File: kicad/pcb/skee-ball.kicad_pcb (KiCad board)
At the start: 2 copper layers, 87 parts, among them J1 SPEAKER_P, J10 NHD_RW, J11 NHD_DB1, J12 NHD_DB0, J13 US_TRIG0, J14 US_TRIG1, J15 US_TRIG2, J16 US_TRIG3, J17 US_TRIG4, J18 US_ECHO0_5, J19 US_ECHO1_5, J2 SPEAKER_N, J20 US_ECH02_5, J21 US_ECHO3_5, J22 US_ECHO4_5, J23 NHD_E1, J24 NHD_E2, J25 NHD_VDD, J26 PWM_SERVO_6, J27 PWM_DC (TIM17_CH1), J28 +24V, J29 NHD_V0, J3 NHD_DB7, J30 BUTTON_P, J31 BUTTON_N, J32 GND, J33 HEADER_GND, J34 HEADER_SWDIO, J35 HEADER_SWCLK, J36 ADC_IN1, J37 3.3, J38 GND, J39 6, J4 NHD_DB6, J40 GND, J41 NHD_VSS, J42 NHD_LED-, J43 NHD_LED+, J5 NHD_DB5, J6 NHD_DB4, J7 NHD_DB3, J8 NHD_DB2, J9 NHD_RS, U1 D24V22F6, U10 LD1117S33TR_SOT223, U11 LD1117S33TR_SOT223, U12 LD1117S33TR_SOT223, U13 LD1117S33TR_SOT223, U14 LD1117S33TR_SOT223, U2 MAX98357A, U3 D24V22F5, U4 STM32F091RCTx, U5 74HC595, U6 74HC595, U7 74LS08, U8 LD1117S33TR_SOT223, U9 LD1117S33TR_SOT223

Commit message: begin routing on pcb
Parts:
- C1, C2, C3, C4, C5, C6, C8: footprint Capacitor_SMD:CP_Elec_3x5.3 -> Capacitor_SMD:C_0805_2012Metric_Pad1.18x1.45mm_HandSolder
- C7, C9: footprint Capacitor_SMD:CP_Elec_3x5.4 -> Capacitor_SMD:C_0805_2012Metric_Pad1.18x1.45mm_HandSolder
- J1, J10, J11, J12, J13, J14, J15, J16, J17, J18, J19, J2, J20, J21, J22, J23, J24, J25, J26, J27, J29, J3, J30, J33, J34, J35, J36, J37, J38, J39, J4, J40, J41, J42, J43, J5, J6, J7, J8, J9: footprint Connector_PinHeader_1.00mm:PinHeader_1x01_P1.00mm_Vertical -> Connector_PinHeader_2.54mm:PinHeader_1x01_P2.54mm_Vertical
- R1, R10, R11, R2, R3, R4, R5, R6, R7, R8, R9, RV1: footprint Resistor_SMD:R_0201_0603Metric -> Resistor_SMD:R_0805_2012Metric_Pad1.20x1.40mm_HandSolder
- moved J22 199.1 mm to (209.5, 55.5)
- moved J21 196.5 mm to (209.5, 51.9)
- moved J20 194.1 mm to (209.5, 48.3)
- moved J19 192.5 mm to (209.5, 44.7)
- moved J18 191.6 mm to (209.5, 41.1)
- moved J33 183.9 mm to (80.2, 86.0)
- moved J34 183.9 mm to (80.2, 79.4)
- moved J35 183.9 mm to (80.2, 82.5)
- moved U12 153.6 mm to (186.9, 76.9), turned to 180 degrees
- moved U11 153.2 mm to (187.0, 65.6), turned to 180 degrees
- moved U10 153.0 mm to (186.9, 54.9), turned to 180 degrees
- moved U9 152.8 mm to (186.8, 43.9), turned to 180 degrees
- moved U8 152.6 mm to (186.7, 33.3), turned to 180 degrees
- moved J13 119.9 mm to (80.2, 61.4)
- moved D5 113.2 mm to (144.8, 65.5)
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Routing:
- net Net-(J22-Pin_1): track 0.00 -> 29.5 mm
- net Net-(J21-Pin_1): track 0.00 -> 24.2 mm
- net Net-(J18-Pin_1): track 0.00 -> 23.8 mm
- net Net-(J20-Pin_1): track 0.00 -> 21.3 mm
- net Net-(J19-Pin_1): track 0.00 -> 20.8 mm

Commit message: added ground plane and some via connections
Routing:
- net GND: track 0.00 -> 129.5 mm, vias 0 -> 13
- added copper zone on B.Cu, net GND

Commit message: update pcb
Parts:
- removed J27: PWM_DC (TIM17_CH1), Connector_PinHeader_2.54mm:PinHeader_1x01_P2.54mm_Vertical
- added C10: 100nF, Capacitor_SMD:C_0805_2012Metric_Pad1.18x1.45mm_HandSolder, B.Cu at (138.4, 64.8)
- added C11: 4.7uF, Capacitor_SMD:C_0805_2012Metric_Pad1.18x1.45mm_HandSolder, B.Cu at (131.7, 61.1)
- added C12: 100nF, Capacitor_SMD:C_0805_2012Metric_Pad1.18x1.45mm_HandSolder, B.Cu at (131.7, 64.4)
- added C14: 100nF, Capacitor_SMD:C_0805_2012Metric_Pad1.18x1.45mm_HandSolder, B.Cu at (138.5, 80.6)
- added C16: 100nF, Capacitor_SMD:C_0805_2012Metric_Pad1.18x1.45mm_HandSolder, B.Cu at (127.3, 75.9)
- added C17: 4.7uF, Capacitor_SMD:C_0805_2012Metric_Pad1.18x1.45mm_HandSolder, B.Cu at (124.6, 76.0)
- added C18: 10nF, Capacitor_SMD:C_0805_2012Metric_Pad1.18x1.45mm_HandSolder, B.Cu at (143.4, 70.4)
- added C19: 1uF, Capacitor_SMD:C_0805_2012Metric_Pad1.18x1.45mm_HandSolder, B.Cu at (145.5, 70.4)
- added J44: HEADER_RST, Connector_PinHeader_2.54mm:PinHeader_1x01_P2.54mm_Vertical, F.Cu at (189.2, 76.2)
- added J45: ULTRASONIC_POWER, Connector_PinHeader_2.54mm:PinHeader_2x05_P2.54mm_Vertical, F.Cu at (124.4, 53.1)
- added J47: DC_GND, Connector_PinHeader_2.54mm:PinHeader_1x01_P2.54mm_Vertical, F.Cu at (55.2, 87.6)
- added J48: PWM_DC, Connector_PinHeader_2.54mm:PinHeader_1x01_P2.54mm_Vertical, F.Cu at (59.9, 87.6)
- added R12: 0, Resistor_SMD:R_0805_2012Metric_Pad1.20x1.40mm_HandSolder, B.Cu at (147.3, 81.3)
- J31: footprint Connector_PinHeader_1.00mm:PinHeader_1x01_P1.00mm_Vertical -> Connector_PinHeader_2.54mm:PinHeader_1x01_P2.54mm_Vertical
- R1: moved to B.Cu
- RV1: footprint Resistor_SMD:R_0805_2012Metric_Pad1.20x1.40mm_HandSolder -> Potentiometer_THT:Potentiometer_Bourns_3339P_Vertical
- U5, U6: footprint Package_SO:SSOP-16_5.3x6.2mm_P0.65mm -> 74HC595N:SOT38-4_NXP
- U7: footprint Package_SO:SSOP-16_5.3x6.2mm_P0.65mm -> SN74LS08N:N14
- moved J26 233.9 mm to (44.3, 87.6), turned to -90 degrees
- moved J39 231.4 mm to (48.0, 87.6), turned to -90 degrees
- moved J40 229.3 mm to (51.6, 87.6), turned to -90 degrees
- moved U7 193.1 mm to (61.6, 73.6), turned to 90 degrees
- moved D8 153.6 mm to (71.5, 76.8)
- moved D6 153.5 mm to (71.5, 73.8)
- moved R10 151.7 mm to (67.6, 77.2)
- moved R8 147.7 mm to (67.6, 73.3)
- moved D7 122.1 mm to (113.8, 53.1), turned to 90 degrees
- moved R11 114.2 mm to (112.4, 81.8)
- moved D9 110.2 mm to (115.6, 82.3)
- moved R9 107.2 mm to (113.9, 56.5), turned to 90 degrees
- moved D4 86.6 mm to (131.7, 86.1), turned to 90 degrees
- moved R6 82.4 mm to (131.7, 82.9), turned to -90 degrees
- moved D1 81.5 mm to (135.5, 86.1), turned to 90 degrees
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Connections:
- net /nRST renamed NRST
- R3 pad 1: PB0 -> PB5
- R4 pad 1: PB1 -> PB6
- R5 pad 1: PB2 -> PB7
- U4 pad 12: GND -> Net-(U4-VSSA)
- U4 pad 13: VDA -> VDD
- U4 pad 25: US_ECHO4_1.1 -> US_ECHO4_3.3
- U4 pad 26: PB0 -> unconnected-(U4-PB0-Pad26)
- U4 pad 27: PB1 -> unconnected-(U4-PB1-Pad27)
- U4 pad 28: PB2 -> unconnected-(U4-PB2-Pad28)
- U4 pad 58: unconnected-(U4-PB6-Pad58) -> PB6
- U4 pad 59: unconnected-(U4-PB7-Pad59) -> PB7
- U4 pad 62: Net-(J27-Pin_1) -> PWM_DC
- U7 pad 1: +6V -> GND
- U7 pad 11: unconnected-(U7-Pad11) -> Net-(J26-Pin_1)
- U7 pad 12: GND -> PWM_SERVO_3.3
- U7 pad 13: GND -> +6V
- U7 pad 2: PWM_SERVO_3.3 -> GND
- U7 pad 3: Net-(J26-Pin_1) -> unconnected-(U7-Pad3)
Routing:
- net GND: track 129.5 -> 20.9 mm, vias 13 -> 2
- net Net-(J11-Pin_1): track 0.00 -> 41.3 mm
- net Net-(J22-Pin_1): track 29.5 -> 0.00 mm
- net Net-(J21-Pin_1): track 24.2 -> 0.00 mm
- net Net-(J18-Pin_1): track 23.8 -> 0.02 mm
- net Net-(J12-Pin_1): track 0.00 -> 22.6 mm
- net Net-(J9-Pin_1): track 0.00 -> 21.5 mm
- net Net-(J20-Pin_1): track 21.3 -> 0.01 mm
- net Net-(J19-Pin_1): track 20.8 -> 0.00 mm
- net Net-(J10-Pin_1): track 0.00 -> 6.09 mm
- net PB3: track 0.00 -> 5.86 mm
- net PB7: track 0.00 -> 5.85 mm
- net Net-(J3-Pin_1): track 0.00 -> 5.65 mm
- net Net-(J8-Pin_1): track 0.00 -> 5.24 mm
- net Net-(J4-Pin_1): track 0.00 -> 5.19 mm
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- added copper zone on F.Cu, net +5V

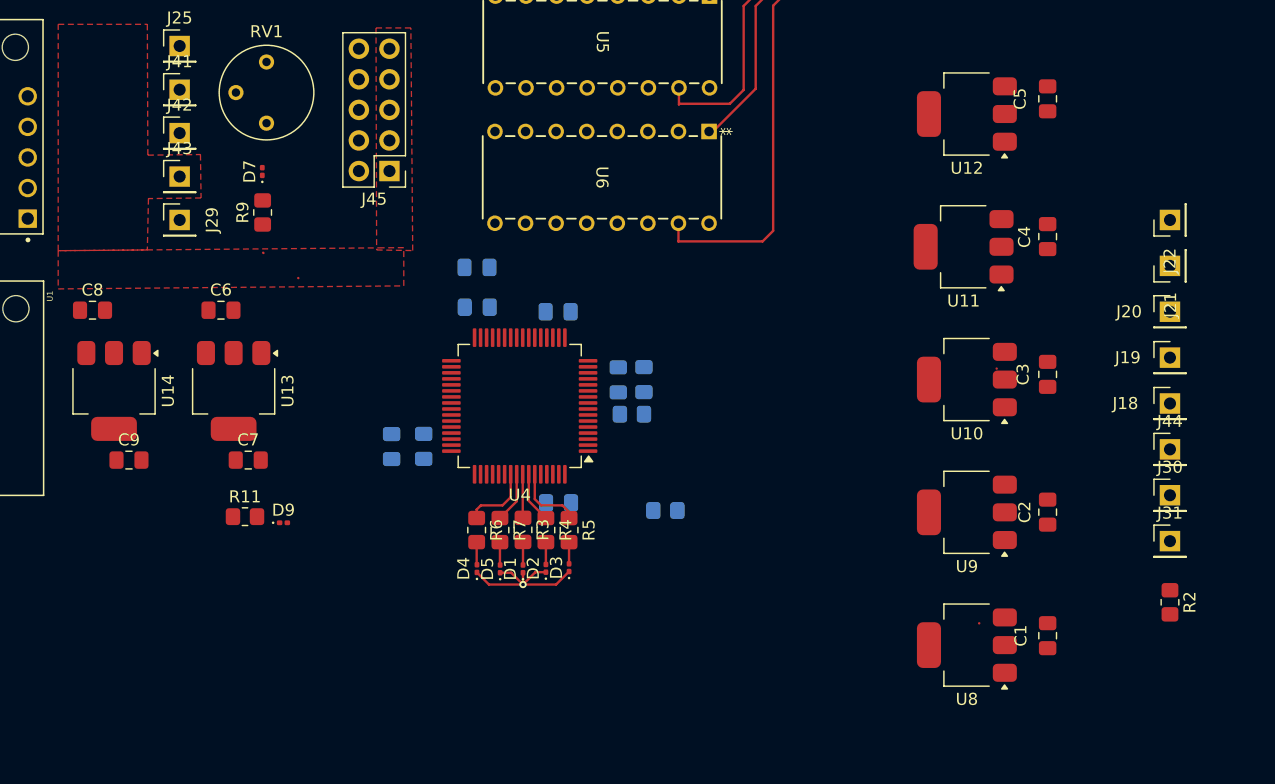
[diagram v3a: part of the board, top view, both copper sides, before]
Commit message: transition to level shifters
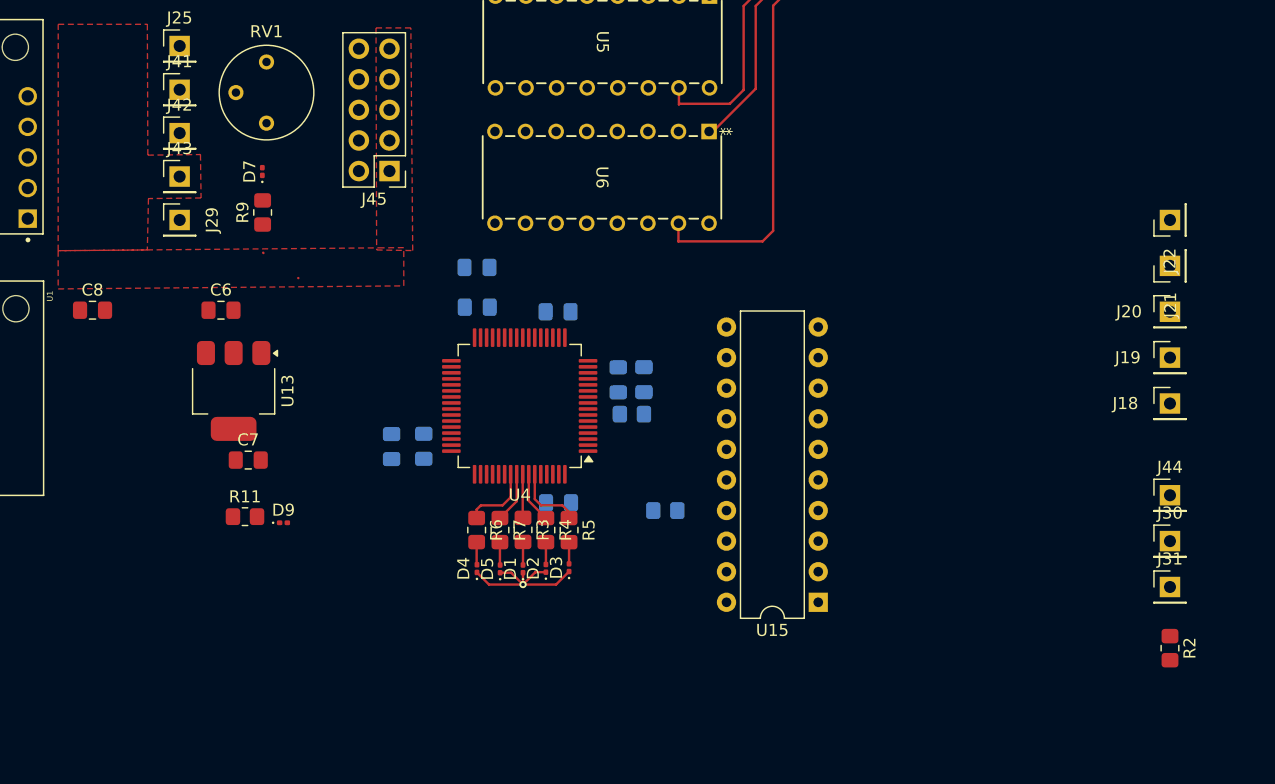
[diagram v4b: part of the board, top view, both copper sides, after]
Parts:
- removed C1, C2, C3, C4, C5: 100nF, Capacitor_SMD:C_0805_2012Metric_Pad1.18x1.45mm_HandSolder
- removed C9: 10uF, Capacitor_SMD:C_0805_2012Metric_Pad1.18x1.45mm_HandSolder
- removed U10, U11, U12, U14, U8, U9: LD1117S33TR_SOT223, Package_TO_SOT_SMD:SOT-223-3_TabPin2
- added U15: 74AHCT541, Package_DIP:DIP-20_W7.62mm, F.Cu at (160.0, 88.9)
- moved J31 3.81 mm to (189.2, 87.6)
- moved J44 3.81 mm to (189.2, 80.0)
- moved J30 3.81 mm to (189.2, 83.8)
- moved R2 3.81 mm to (189.2, 92.7)
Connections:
- U4 pad 10: US_ECHO1_3.3 -> US_ECHO2_3.3
- U4 pad 11: US_ECHO2_3.3 -> US_ECHO1_3.3
- U4 pad 13: VDD -> VDDA
- U4 pad 14: unconnected-(U4-PA0-Pad14) -> US_ECHO0_3.3
- U4 pad 24: US_ECHO3_3.3 -> unconnected-(U4-PC4-Pad24)
- U4 pad 25: US_ECHO4_3.3 -> unconnected-(U4-PC5-Pad25)
- U4 pad 8: unconnected-(U4-PC0-Pad8) -> US_ECHO4_3.3
- U4 pad 9: US_ECHO0_3.3 -> US_ECHO3_3.3

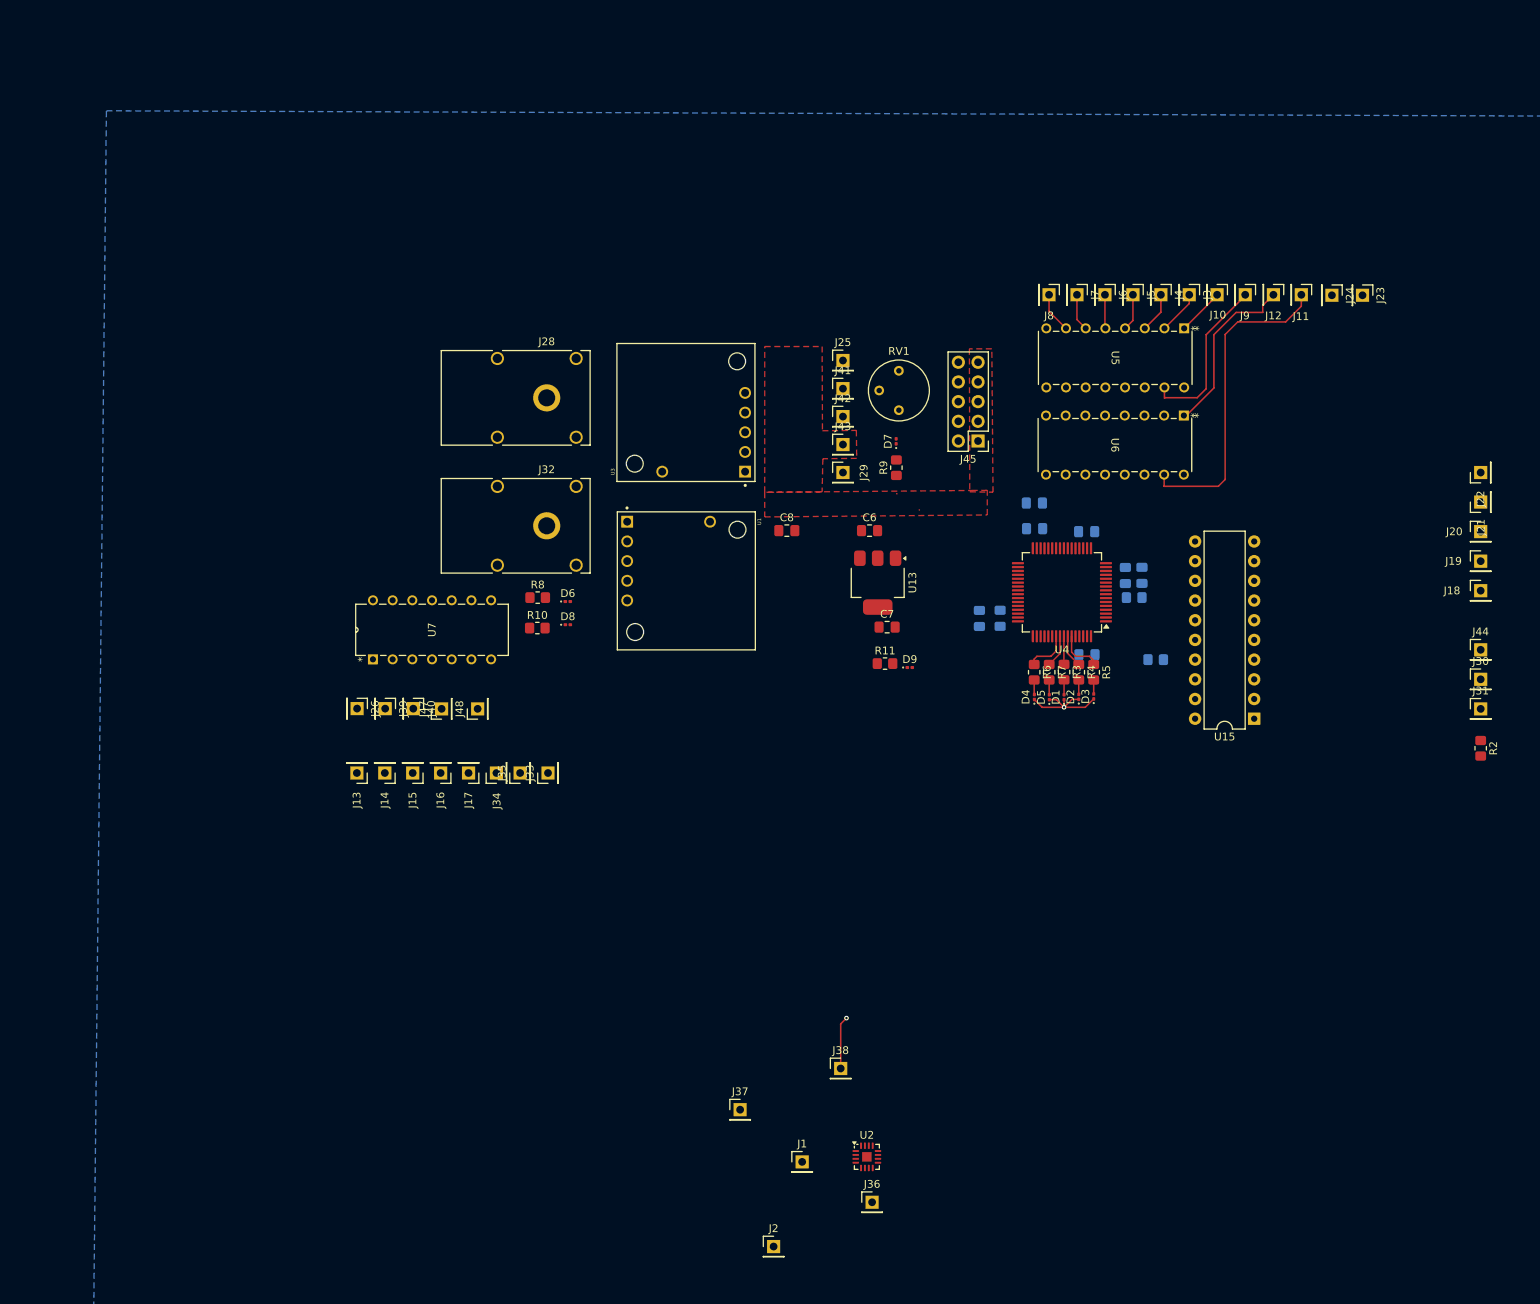
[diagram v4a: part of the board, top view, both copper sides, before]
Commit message: add new connector footprints
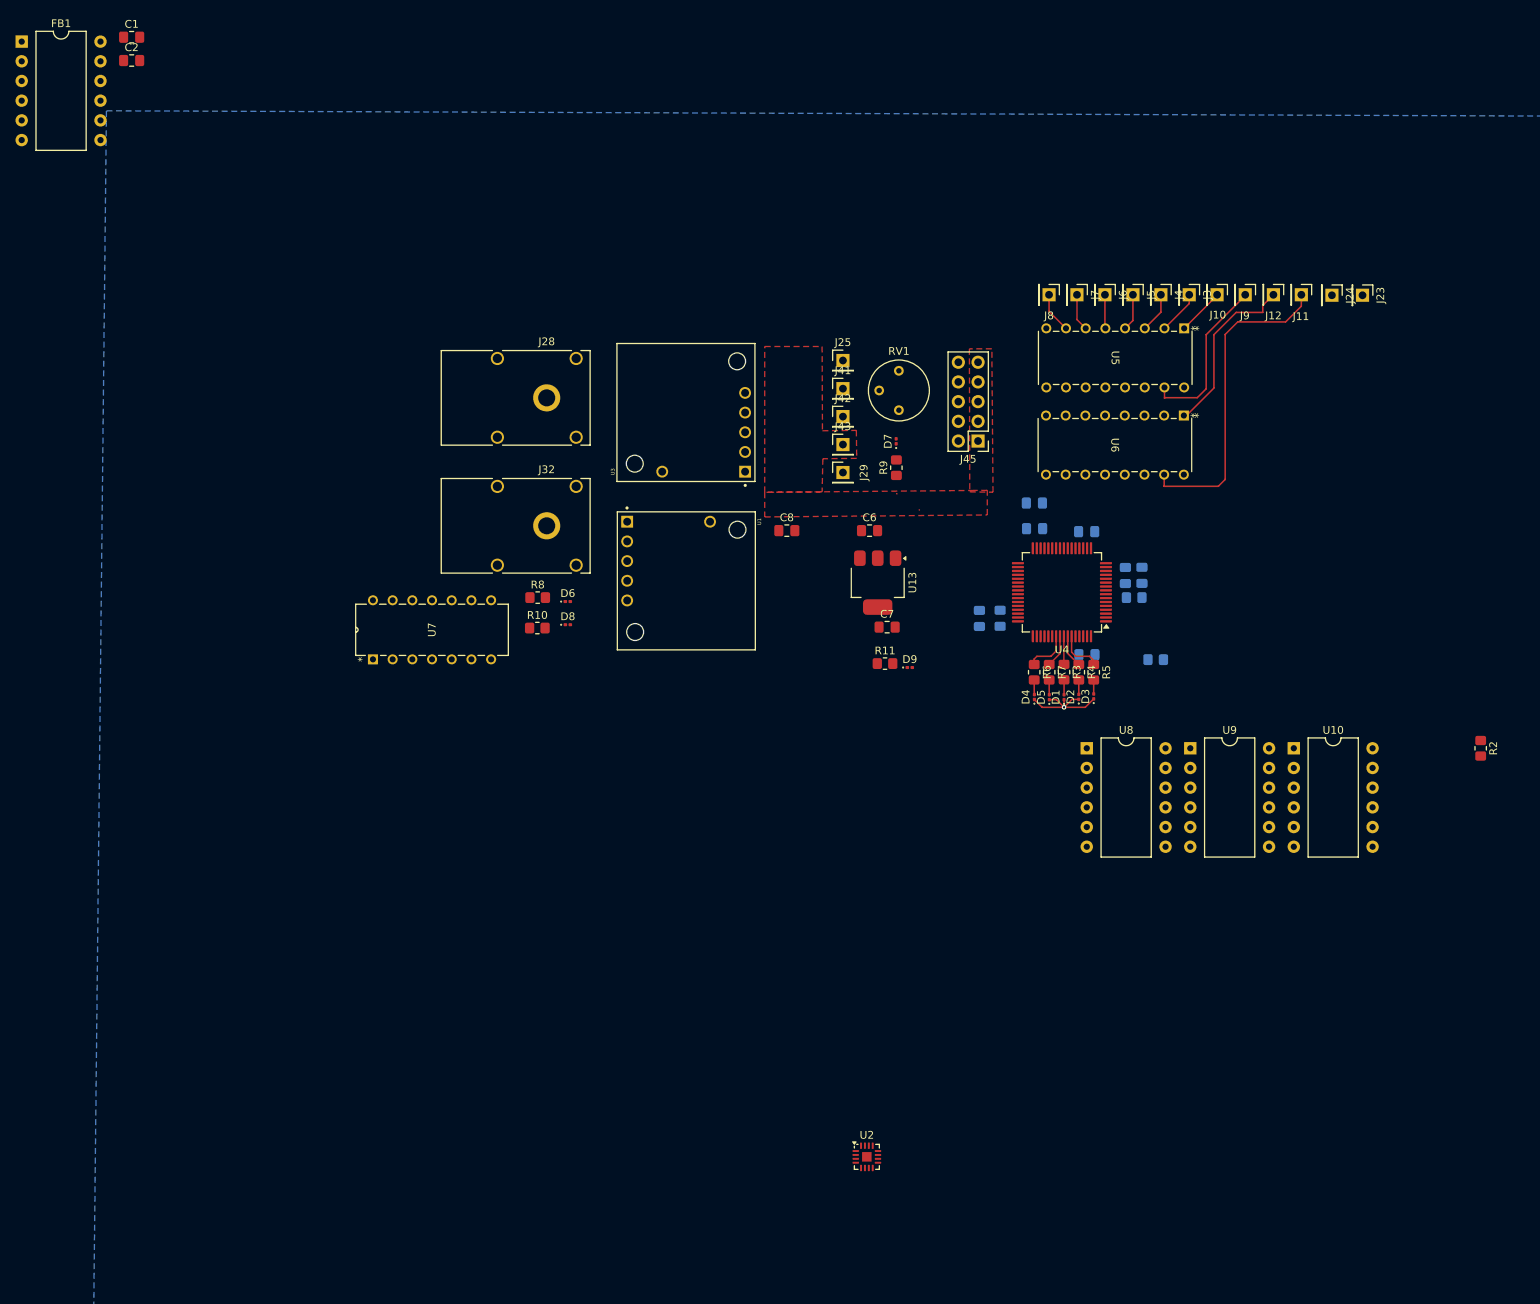
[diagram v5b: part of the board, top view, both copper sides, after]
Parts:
- removed J1: SPEAKER_P, Connector_PinHeader_2.54mm:PinHeader_1x01_P2.54mm_Vertical
- removed J13: US_TRIG0, Connector_PinHeader_2.54mm:PinHeader_1x01_P2.54mm_Vertical
- removed J14: US_TRIG1, Connector_PinHeader_2.54mm:PinHeader_1x01_P2.54mm_Vertical
- removed J15: US_TRIG2, Connector_PinHeader_2.54mm:PinHeader_1x01_P2.54mm_Vertical
- removed J16: US_TRIG3, Connector_PinHeader_2.54mm:PinHeader_1x01_P2.54mm_Vertical
- removed J17: US_TRIG4, Connector_PinHeader_2.54mm:PinHeader_1x01_P2.54mm_Vertical
- removed J18: US_ECHO0_5, Connector_PinHeader_2.54mm:PinHeader_1x01_P2.54mm_Vertical
- removed J19: US_ECHO1_5, Connector_PinHeader_2.54mm:PinHeader_1x01_P2.54mm_Vertical
- removed J2: SPEAKER_N, Connector_PinHeader_2.54mm:PinHeader_1x01_P2.54mm_Vertical
- removed J20: US_ECH02_5, Connector_PinHeader_2.54mm:PinHeader_1x01_P2.54mm_Vertical
- removed J21: US_ECHO3_5, Connector_PinHeader_2.54mm:PinHeader_1x01_P2.54mm_Vertical
- removed J22: US_ECHO4_5, Connector_PinHeader_2.54mm:PinHeader_1x01_P2.54mm_Vertical
- removed J26: PWM_SERVO_6, Connector_PinHeader_2.54mm:PinHeader_1x01_P2.54mm_Vertical
- removed J30: BUTTON_P, Connector_PinHeader_2.54mm:PinHeader_1x01_P2.54mm_Vertical
- removed J31: BUTTON_N, Connector_PinHeader_2.54mm:PinHeader_1x01_P2.54mm_Vertical
- removed J33: HEADER_GND, Connector_PinHeader_2.54mm:PinHeader_1x01_P2.54mm_Vertical
- removed J34: HEADER_SWDIO, Connector_PinHeader_2.54mm:PinHeader_1x01_P2.54mm_Vertical
- removed J35: HEADER_SWCLK, Connector_PinHeader_2.54mm:PinHeader_1x01_P2.54mm_Vertical
- removed J36: ADC_IN1, Connector_PinHeader_2.54mm:PinHeader_1x01_P2.54mm_Vertical
- removed J37: 3.3, Connector_PinHeader_2.54mm:PinHeader_1x01_P2.54mm_Vertical
- removed J38, J40: GND, Connector_PinHeader_2.54mm:PinHeader_1x01_P2.54mm_Vertical
- removed J39: 6, Connector_PinHeader_2.54mm:PinHeader_1x01_P2.54mm_Vertical
- removed J44: HEADER_RST, Connector_PinHeader_2.54mm:PinHeader_1x01_P2.54mm_Vertical
- removed J47: DC_GND, Connector_PinHeader_2.54mm:PinHeader_1x01_P2.54mm_Vertical
- removed J48: PWM_DC, Connector_PinHeader_2.54mm:PinHeader_1x01_P2.54mm_Vertical
- removed U15: 74AHCT541, Package_DIP:DIP-20_W7.62mm
- added C1: 10nF, Capacitor_SMD:C_0805_2012Metric_Pad1.18x1.45mm_HandSolder, F.Cu at (15.3, 1.00)
- added C2: 1uF, Capacitor_SMD:C_0805_2012Metric_Pad1.18x1.45mm_HandSolder, F.Cu at (15.3, 4.01)
- added FB1: FerriteBead, Package_DIP:DIP-12_W10.16mm, F.Cu at (1.07, 1.57)
- added U10: ~, Package_DIP:DIP-12_W10.16mm, F.Cu at (165.1, 92.7)
- added U8: ~, Package_DIP:DIP-12_W10.16mm, F.Cu at (138.4, 92.7)
- added U9: ~, Package_DIP:DIP-12_W10.16mm, F.Cu at (151.8, 92.7)
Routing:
- net GND: track 20.9 -> 14.1 mm, vias 2 -> 1
